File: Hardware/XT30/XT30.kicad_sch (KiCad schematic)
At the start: 1 part, among them J1 XT30PW-F

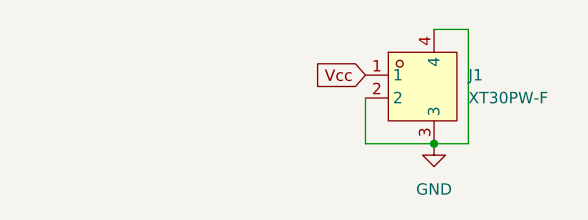
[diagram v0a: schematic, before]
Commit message: Found the male XT30 & improved the XT30 board
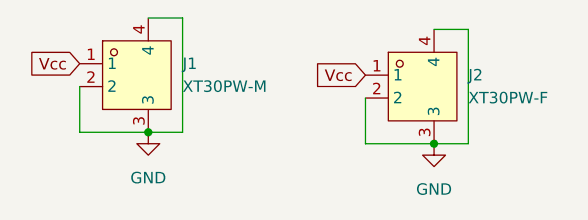
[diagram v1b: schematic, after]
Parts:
- added J1: XT30PW-M, tinker:AMASS_XT30PW-M, symbol New_Library:XT30PW-M
- J2: renamed from J1; footprint tinker:CONN-TH_XT30PW-F-1 -> tinker:AMASS_XT30PW-F
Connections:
- net GND: now also J1.2, J1.3, J1.4
- net Vcc: now also J1.1
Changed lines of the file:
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@@
   (junction (at 93.98 85.09) (diameter 0) (color 0 0 0 0)
+  )
+  (junction (at 62.23 83.82) (diameter 0) (color 0 0 0 0)
+  )
+  (wire (pts (xy 54.61 78.74) (xy 54.61 83.82))
+    (stroke (width 0) (type default) (color 0 0 0 0))
   )
   (wire (pts (xy 86.36 85.09) (xy 93.98 85.09))
@@
     (stroke (width 0) (type default) (color 0 0 0 0))
   )
+  (wire (pts (xy 66.04 83.82) (xy 62.23 83.82))
+    (stroke (width 0) (type default) (color 0 0 0 0))
+  )
+  (wire (pts (xy 66.04 71.12) (xy 66.04 83.82))
+    (stroke (width 0) (type default) (color 0 0 0 0))
+  )
+  (wire (pts (xy 54.61 83.82) (xy 62.23 83.82))
+    (stroke (width 0) (type default) (color 0 0 0 0))
+  )
   (wire (pts (xy 97.79 85.09) (xy 93.98 85.09))
+    (stroke (width 0) (type default) (color 0 0 0 0))
+  )
+  (wire (pts (xy 62.23 71.12) (xy 66.04 71.12))
     (stroke (width 0) (type default) (color 0 0 0 0))
   )
@@
     (effects (font (size 1.27 1.27)) (justify right))
     (property "Intersheet References" "${INTERSHEET_REFS}" (id 0) (at 80.6812 77.3906 0)
+      (effects (font (size 1.27 1.27)) (justify right) hide)
+    )
+  )
+  (global_label "Vcc" (shape input) (at 54.61 76.2 180) (fields_autoplaced)
+    (effects (font (size 1.27 1.27)) (justify right))
+    (property "Intersheet References" "${INTERSHEET_REFS}" (id 0) (at 48.9312 76.1206 0)
       (effects (font (size 1.27 1.27)) (justify right) hide)
     )
@@
     (pin "1")
   )
+  (symbol (lib_id "New_Library:XT30PW-M") (at 59.69 77.47 0) (unit 1)
+    (in_bom yes) (on_board yes) (fields_autoplaced)
+    (property "Reference" "J1" (id 0) (at 66.04 76.1999 0)
+      (effects (font (size 1.27 1.27)) (justify left))
+    )
+    (property "Value" "XT30PW-M" (id 1) (at 66.04 78.7399 0)
+      (effects (font (size 1.27 1.27)) (justify left))
+    )
+    (property "Footprint" "tinker:AMASS_XT30PW-M" (id 2) (at 59.69 91.44 0)
+      (effects (font (size 1.27 1.27)) hide)
+    )
+    (property "Datasheet" "" (id 3) (at 59.69 77.47 0)
+      (effects (font (size 1.27 1.27)) hide)
+    )
+    (property "LCSC Part" "C2913282" (id 4) (at 59.69 93.98 0)
+      (effects (font (size 1.27 1.27)) hide)
+    )
+    (pin "1")
+    (pin "2")
+    (pin "3")
+    (pin "4")
+  )
   (symbol (lib_id "New_Library:XT30PW-F") (at 91.44 78.74 0) (unit 1)
     (in_bom yes) (on_board yes) (fields_autoplaced)
-    (property "Reference" "J1" (id 0) (at 97.79 77.4699 0)
+    (property "Reference" "J2" (id 0) (at 97.79 77.4699 0)
       (effects (font (size 1.27 1.27)) (justify left))
     )
@@
       (effects (font (size 1.27 1.27)) (justify left))
     )
-    (property "Footprint" "tinker:CONN-TH_XT30PW-F-1" (id 2) (at 91.44 92.71 0)
+    (property "Footprint" "tinker:AMASS_XT30PW-F" (id 2) (at 91.44 92.71 0)
       (effects (font (size 1.27 1.27)) hide)
     )
@@
     (pin "4")
   )
+  (symbol (lib_id "power:GND") (at 62.23 83.82 0) (unit 1)
+    (in_bom yes) (on_board yes) (fields_autoplaced)
+    (property "Reference" "#PWR0102" (id 0) (at 62.23 90.17 0)
+      (effects (font (size 1.27 1.27)) hide)
+    )
+    (property "Value" "GND" (id 1) (at 62.23 88.9 0))
+    (property "Footprint" "" (id 2) (at 62.23 83.82 0)
+      (effects (font (size 1.27 1.27)) hide)
+    )
+    (property "Datasheet" "" (id 3) (at 62.23 83.82 0)
+      (effects (font (size 1.27 1.27)) hide)
+    )
+    (pin "1")
+  )
   (sheet_instances
     (path "/" (page "1"))
@@
       (reference "#PWR0101") (unit 1) (value "GND") (footprint "")
     )
+    (path "/fb338914-5868-4816-950a-b530543c17c7"
+      (reference "#PWR0102") (unit 1) (value "GND") (footprint "")
+    )
+    (path "/59a14851-45a6-4c11-b2cd-b42abb0c9a2e"
+      (reference "J1") (unit 1) (value "XT30PW-M") (footprint "tinker:AMASS_XT30PW-M")
+    )
     (path "/f765a63a-6f0e-4366-a5d7-eae8d1fe2b74"
-      (reference "J1") (unit 1) (value "XT30PW-F") (footprint "tinker:CONN-TH_XT30PW-F-1")
+      (reference "J2") (unit 1) (value "XT30PW-F") (footprint "tinker:AMASS_XT30PW-F")
     )
   )
